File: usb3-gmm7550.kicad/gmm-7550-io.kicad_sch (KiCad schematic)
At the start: 17 parts, among them J4 10144517-061802LF, SW2 SW_Push, SW3 SW_Push

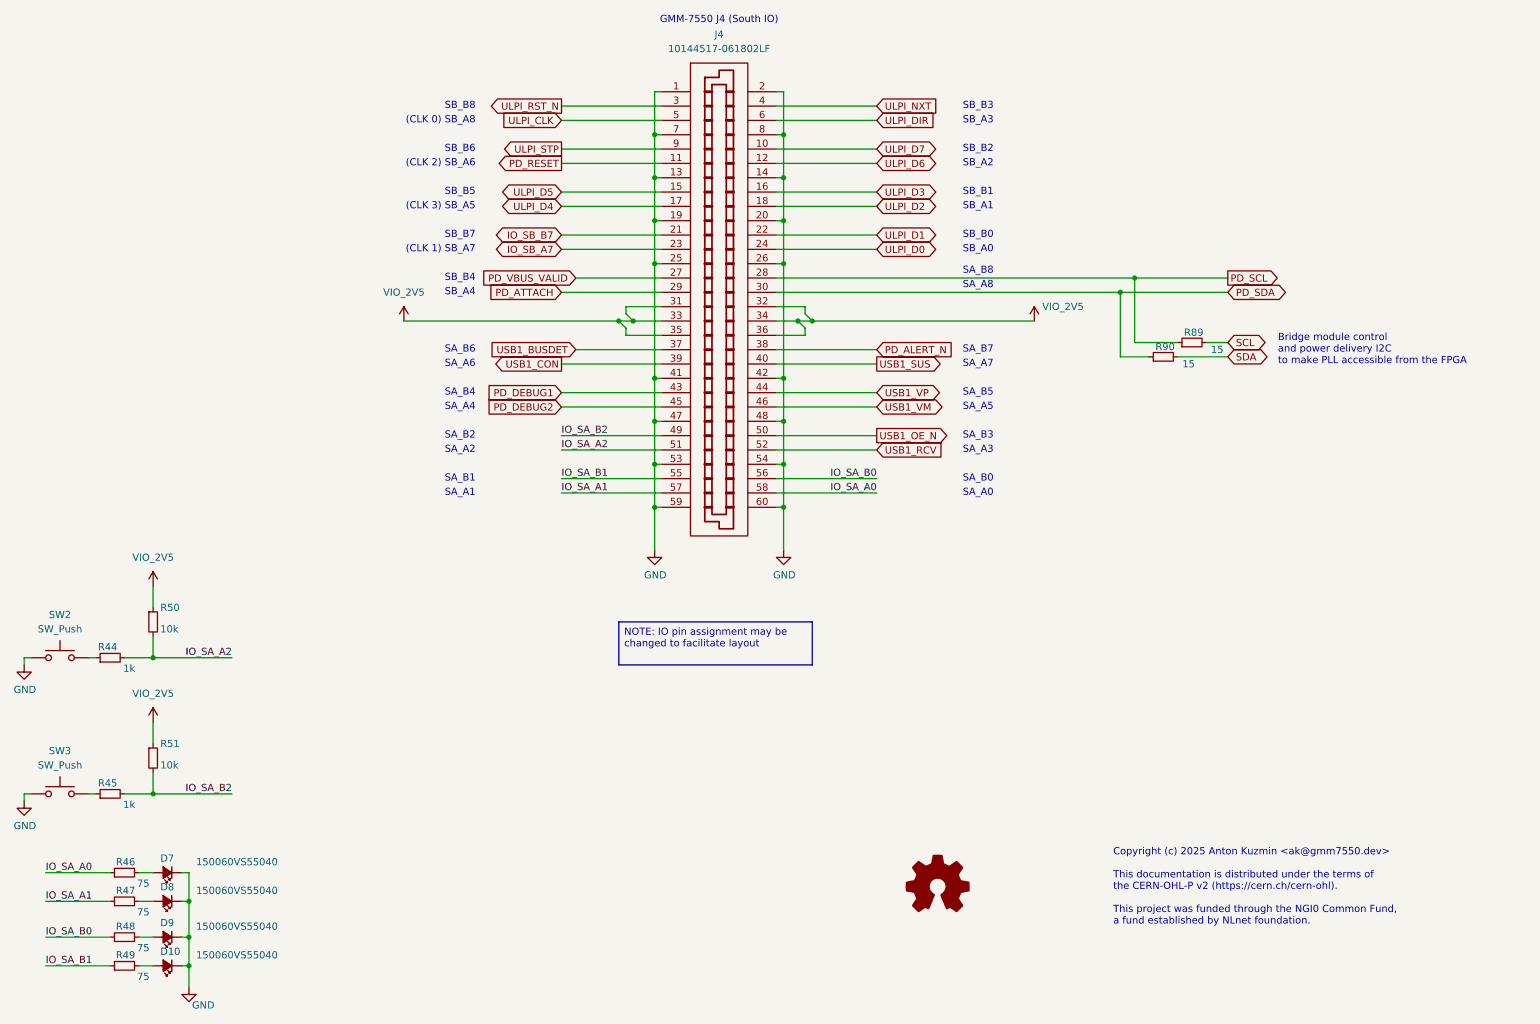
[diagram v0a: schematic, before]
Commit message: Layout -- suffling FPGA IOs (LEDs, buttons)
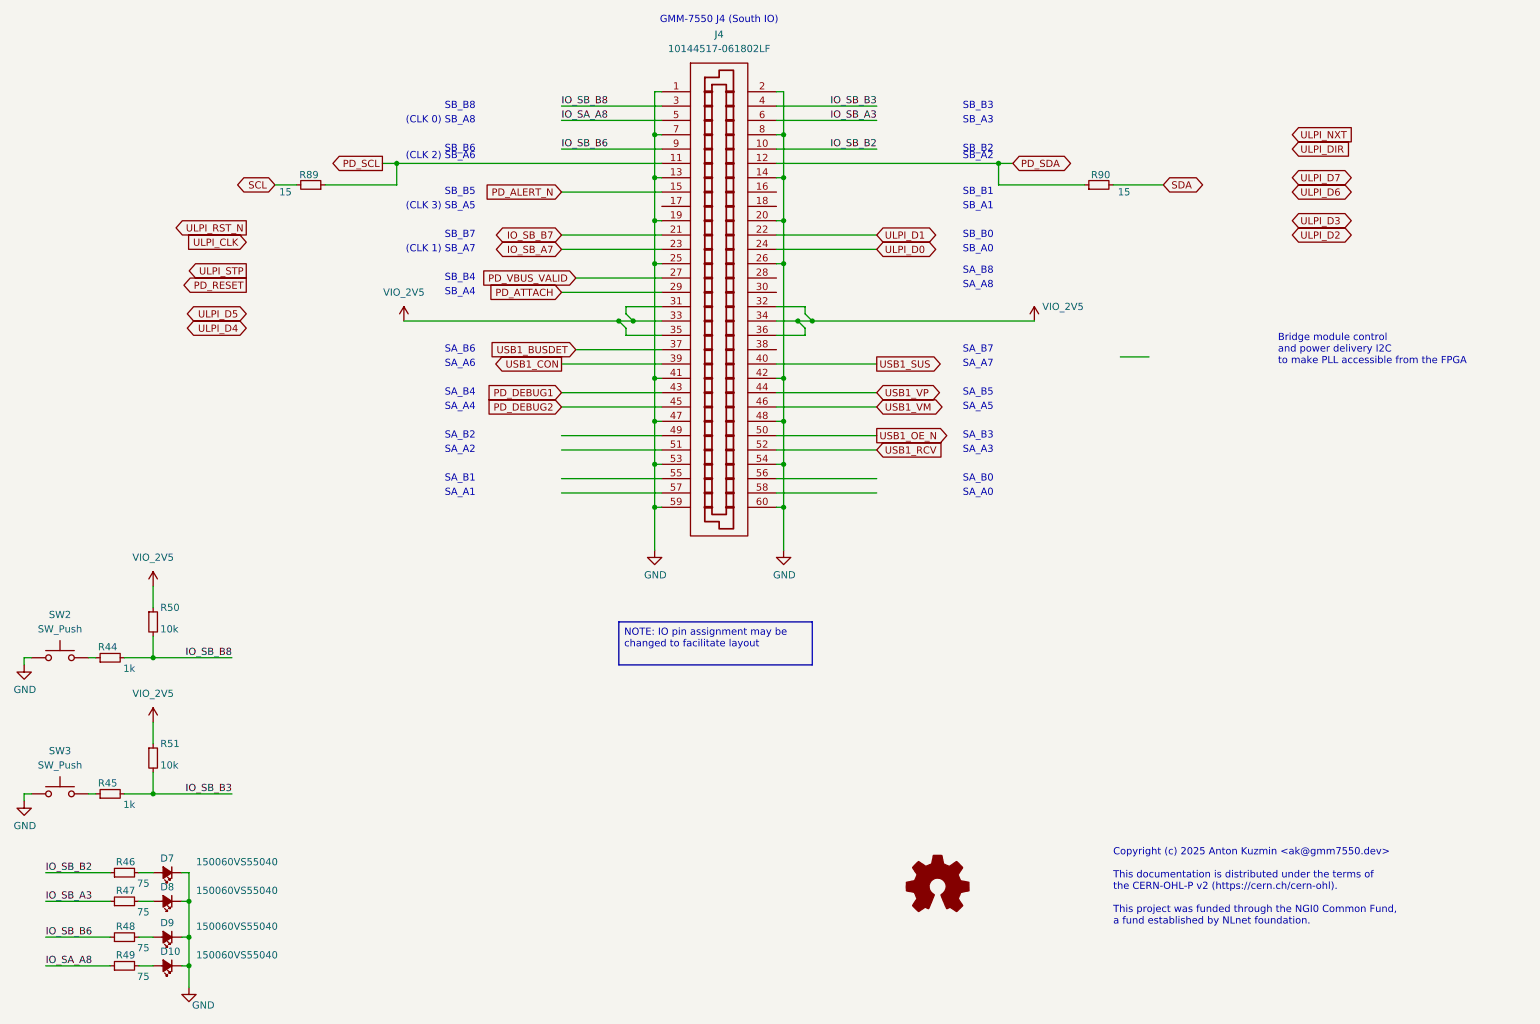
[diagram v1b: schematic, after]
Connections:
- net PD_ALERT_N: now also J4.15; no longer J4.38
- net PD_RESET: no longer J4.11
- net PD_SCL: now also J4.11; no longer J4.28
- net PD_SDA: now also J4.12; no longer J4.30
- net ULPI_CLK: no longer J4.5
- net ULPI_D2: no longer J4.18
- net ULPI_D3: no longer J4.16
- net ULPI_D4: no longer J4.17
- net ULPI_D5: no longer J4.15
- net ULPI_D6: no longer J4.12
- net ULPI_D7: no longer J4.10
- net ULPI_DIR: no longer J4.6
- net ULPI_NXT: no longer J4.4
- net ULPI_RST_N: no longer J4.3
- net ULPI_STP: no longer J4.9
- net IO_SA_A0: no longer names the net of J4.58
- net IO_SA_A0: no longer R46.1
- net IO_SA_A1: no longer names the net of J4.57
- net IO_SA_A1: no longer R47.1
- net IO_SA_A2 renamed IO_SB_B8
- net IO_SB_B8: now also J4.3; no longer J4.51
- net IO_SA_B0: no longer names the net of J4.56
- net IO_SA_B0: no longer R48.1
- net IO_SA_B1: no longer names the net of J4.55
- net IO_SA_B1: no longer R49.1
- net IO_SA_B2 renamed IO_SB_B3
- net IO_SB_B3: now also J4.4; no longer J4.49
- new net IO_SA_A8: J4.5, R49.1
- new net IO_SB_A3: J4.6, R47.1
- new net IO_SB_B2: J4.10, R46.1
- new net IO_SB_B6: J4.9, R48.1
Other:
- moved on the sheet: R89, R90

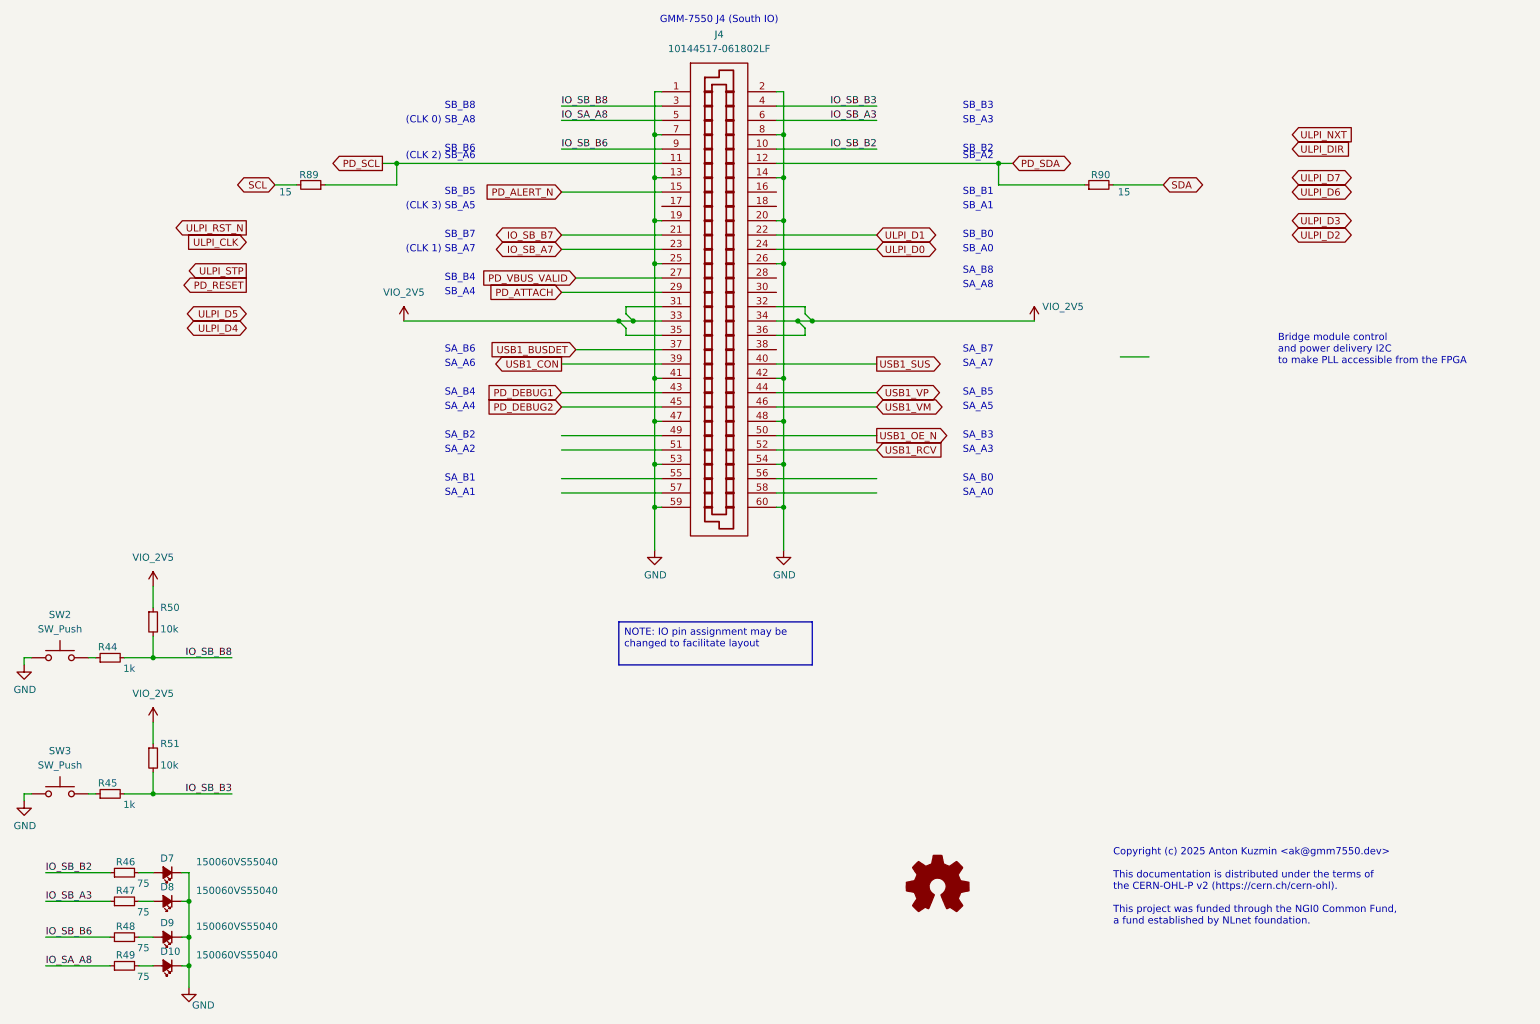
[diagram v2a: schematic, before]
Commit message: Layout -- re-arrange and connect all GMM-7550 IOs on J4 (USB 1.1 and 2.0)
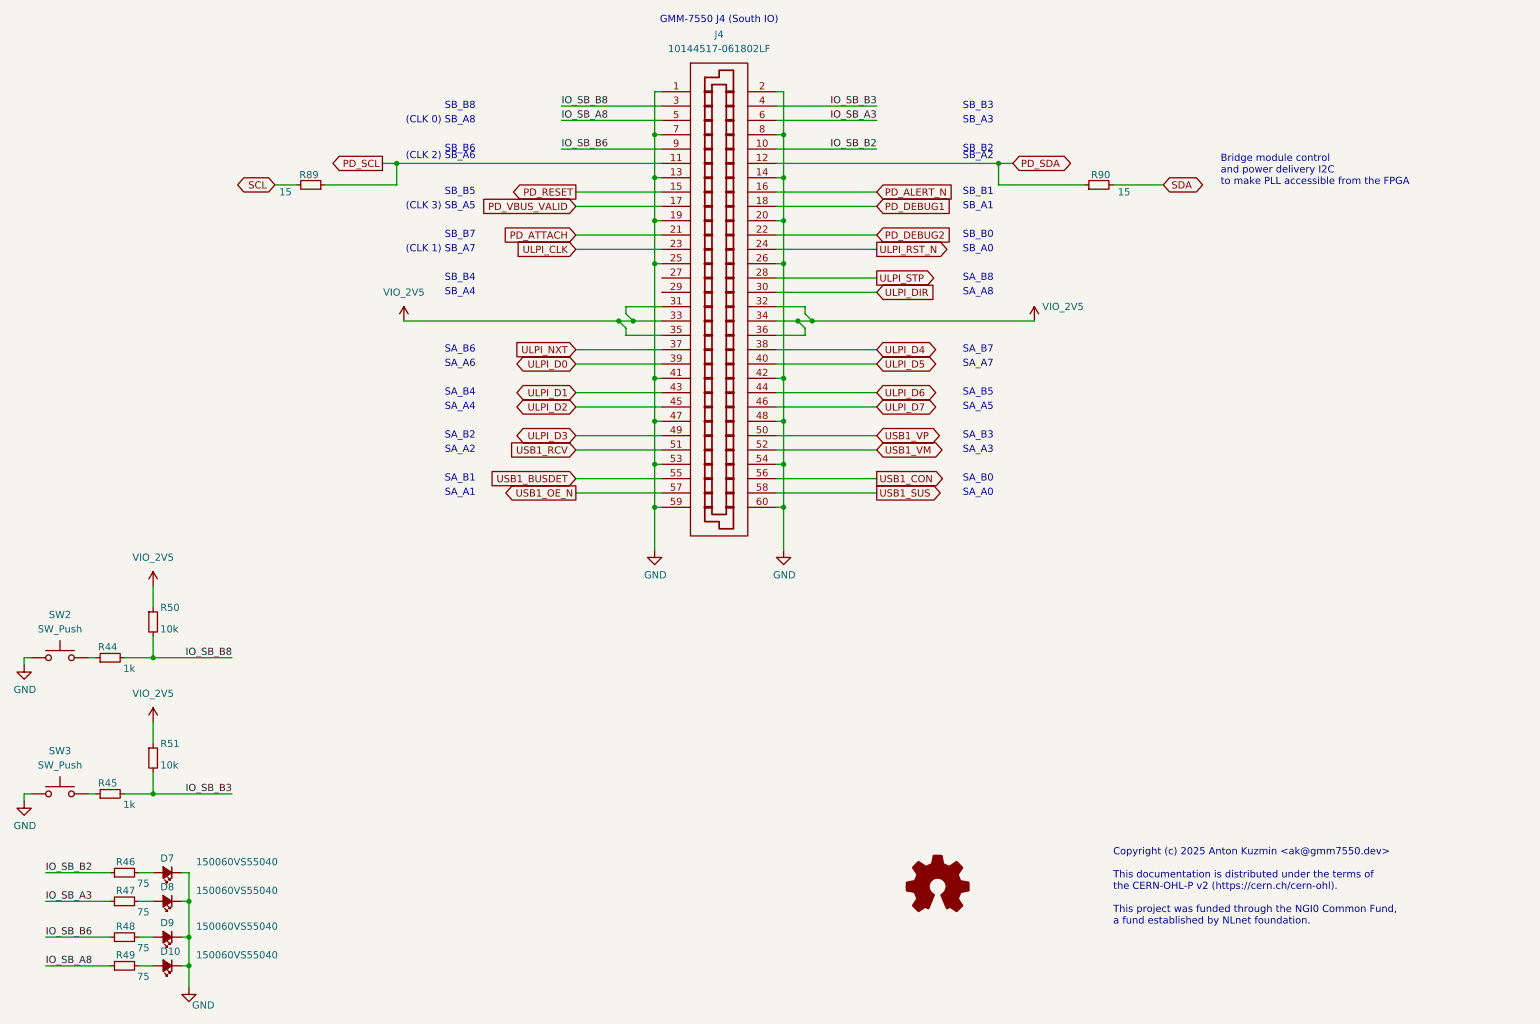
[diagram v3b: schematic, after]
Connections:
- net IO_SB_A7 is gone; now on net ULPI_CLK: J4.23
- net IO_SB_B7 is gone; now on net PD_ATTACH: J4.21
- net PD_ALERT_N: now also J4.16; no longer J4.15
- net PD_ATTACH: no longer J4.29
- net PD_DEBUG1: now also J4.18; no longer J4.43
- net PD_DEBUG2: now also J4.22; no longer J4.45
- net PD_RESET: now also J4.15
- net PD_VBUS_VALID: now also J4.17; no longer J4.27
- net ULPI_D0: now also J4.39; no longer J4.24
- net ULPI_D1: now also J4.43; no longer J4.22
- net ULPI_D2: now also J4.45
- net ULPI_D3: now also J4.49
- net ULPI_D4: now also J4.38
- net ULPI_D5: now also J4.40
- net ULPI_D6: now also J4.44
- net ULPI_D7: now also J4.46
- net ULPI_DIR: now also J4.30
- net ULPI_NXT: now also J4.37
- net ULPI_RST_N: now also J4.24
- net ULPI_STP: now also J4.28
- net USB1_BUSDET: now also J4.55; no longer J4.37
- net USB1_CON: now also J4.56; no longer J4.39
- net USB1_OE_N: now also J4.57; no longer J4.50
- net USB1_RCV: now also J4.51; no longer J4.52
- net USB1_SUS: now also J4.58; no longer J4.40
- net USB1_VM: now also J4.52; no longer J4.46
- net USB1_VP: now also J4.50; no longer J4.44
- net IO_SA_A8 renamed IO_SB_A8

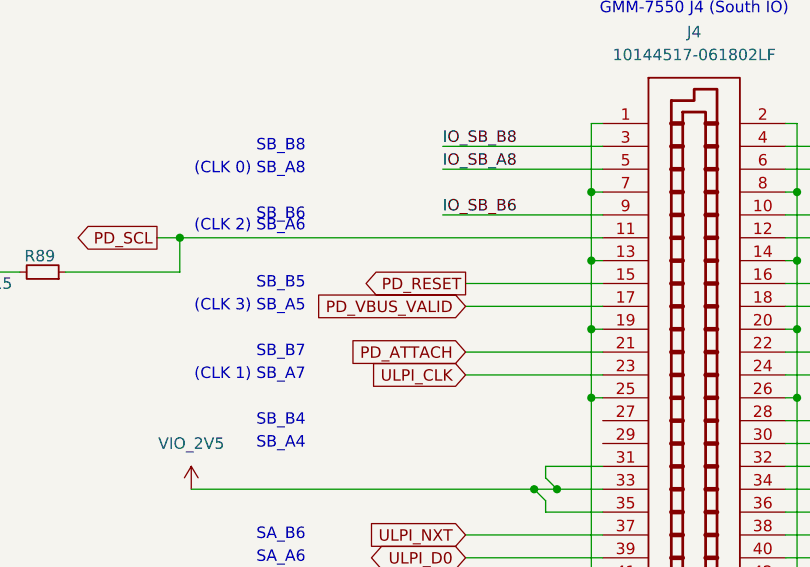
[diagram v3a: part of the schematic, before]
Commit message: USB Power Delivery redesign (STmicro controller is NRND)
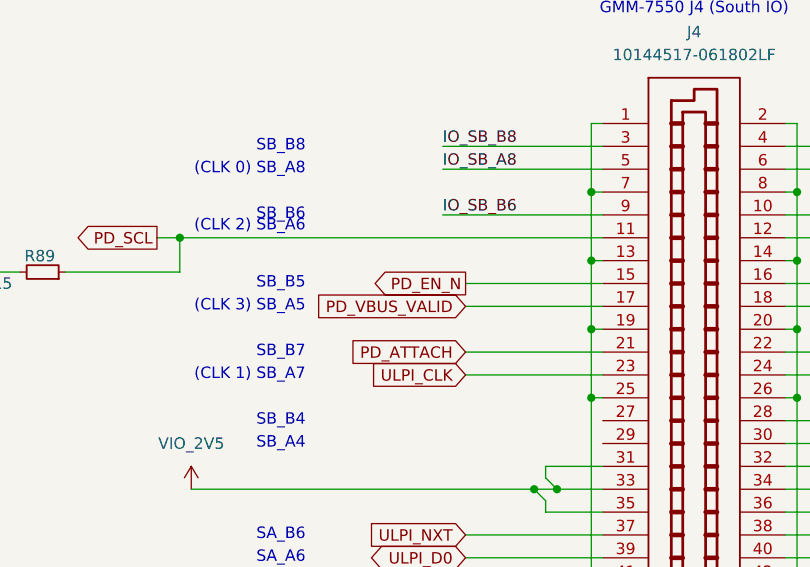
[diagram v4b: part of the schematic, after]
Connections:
- net PD_RESET renamed PD_EN_N
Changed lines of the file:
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@@
 	(title_block
 		(title "GMM-7550 USB3 Adapter")
-		(date "2025-09-xx")
-		(rev "0.9.4")
+		(date "2025-10-01")
+		(rev "0.9.5")
 	)
 	(text "SB_B7"
@@
 		)
 	)
-	(global_label "PD_RESET"
+	(global_label "PD_EN_N"
 		(shape output)
 		(at 119.38 50.8 180)
@@
 		)
 		(property "Intersheetrefs" "${INTERSHEET_REFS}"
-			(at 107.1421 50.8 0)
+			(at 108.1096 50.8 0)
 			(effects
 				(font

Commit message: Layout WIP: split power plane (internal layer 2)
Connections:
- net PD_ATTACH renamed PD_SRC_EN
- net PD_DEBUG1 renamed IO_SB_A1
- net PD_DEBUG2 renamed PD_DISCH
- net PD_VBUS_VALID renamed IO_SB_A5
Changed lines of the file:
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@@
-		)
-	)
-	(global_label "PD_VBUS_VALID"
-		(shape input)
-		(at 119.38 53.34 180)
-		(fields_autoplaced yes)
-		(effects
-			(font
-				(size 1.27 1.27)
-			)
-			(justify right)
-		)
-		(property "Intersheetrefs" "${INTERSHEET_REFS}"
-			(at 101.9409 53.34 0)
-			(effects
-				(font
-					(size 1.27 1.27)
-				)
-				(justify right)
-				(hide yes)
-			)
 		)
 	)
@@
 		)
 	)
-	(global_label "PD_ATTACH"
-		(shape input)
-		(at 119.38 58.42 180)
-		(fields_autoplaced yes)
-		(effects
-			(font
-				(size 1.27 1.27)
-			)
-			(justify right)
-		)
-		(property "Intersheetrefs" "${INTERSHEET_REFS}"
-			(at 106.1743 58.42 0)
-			(effects
-				(font
-					(size 1.27 1.27)
-				)
-				(justify right)
-				(hide yes)
-			)
-		)
-	)
 	(global_label "ULPI_RST_N"
 		(shape output)
@@
 		(property "Intersheetrefs" "${INTERSHEET_REFS}"
 			(at 230.3716 49.53 0)
-			(effects
-				(font
-					(size 1.27 1.27)
-				)
-				(justify left)
-				(hide yes)
-			)
-		)
-	)
-	(global_label "PD_DEBUG2"
-		(shape input)
-		(at 172.72 58.42 0)
-		(fields_autoplaced yes)
-		(effects
-			(font
-				(size 1.27 1.27)
-			)
-			(justify left)
-		)
-		(property "Intersheetrefs" "${INTERSHEET_REFS}"
-			(at 186.7118 58.42 0)
 			(effects
 				(font
@@
 		)
 	)
+	(global_label "PD_SRC_EN"
+		(shape output)
+		(at 119.38 58.42 180)
+		(fields_autoplaced yes)
+		(effects
+			(font
+				(size 1.27 1.27)
+			)
+			(justify right)
+		)
+		(property "Intersheetrefs" "${INTERSHEET_REFS}"
+			(at 105.6906 58.42 0)
+			(effects
+				(font
+					(size 1.27 1.27)
+				)
+				(justify right)
+				(hide yes)
+			)
+		)
+	)
 	(global_label "USB1_CON"
 		(shape output)
@@
 		)
 	)
+	(global_label "PD_DISCH"
+		(shape output)
+		(at 172.72 58.42 0)
+		(fields_autoplaced yes)
+		(effects
+			(font
+				(size 1.27 1.27)
+			)
+			(justify left)
+		)
+		(property "Intersheetrefs" "${INTERSHEET_REFS}"
+			(at 184.8976 58.42 0)
+			(effects
+				(font
+					(size 1.27 1.27)
+				)
+				(justify left)
+				(hide yes)
+			)
+		)
+	)
 	(global_label "USB1_BUSDET"
 		(shape input)
@@
 		)
 	)
+	(global_label "IO_SB_A5"
+		(shape bidirectional)
+		(at 119.38 53.34 180)
+		(fields_autoplaced yes)
+		(effects
+			(font
+				(size 1.27 1.27)
+			)
+			(justify right)
+		)
+		(property "Intersheetrefs" "${INTERSHEET_REFS}"
+			(at 106.6354 53.34 0)
+			(effects
+				(font
+					(size 1.27 1.27)
+				)
+				(justify right)
+				(hide yes)
+			)
+		)
+	)
 	(global_label "PD_ALERT_N"
 		(shape input)
@@
 		)
 	)
-	(global_label "PD_DEBUG1"
-		(shape input)
+	(global_label "IO_SB_A1"
+		(shape bidirectional)
 		(at 172.72 53.34 0)
 		(fields_autoplaced yes)
@@
 		)
 		(property "Intersheetrefs" "${INTERSHEET_REFS}"
-			(at 186.7118 53.34 0)
-			(effects
-				(font
+			(at 185.4646 53.34 0)
+			(effects
+				(font
